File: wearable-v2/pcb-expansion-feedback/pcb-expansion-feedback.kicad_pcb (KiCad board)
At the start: 2 copper layers, 35.1 x 19 mm, 30 parts, among them J16 EA_WF030-39S, J17 JST_AUDIO_OUT, J18 DEBUG_HERALD, J19 FTDI_HERALD, J9 HERALD_V2_CONN_PLUG, U10 ATmega328PB-M, U13 TPA6139A2RGTR, U16 DRV2605LDGSR, U5 MX25R6435FZNIL0, Y2 8Mhz

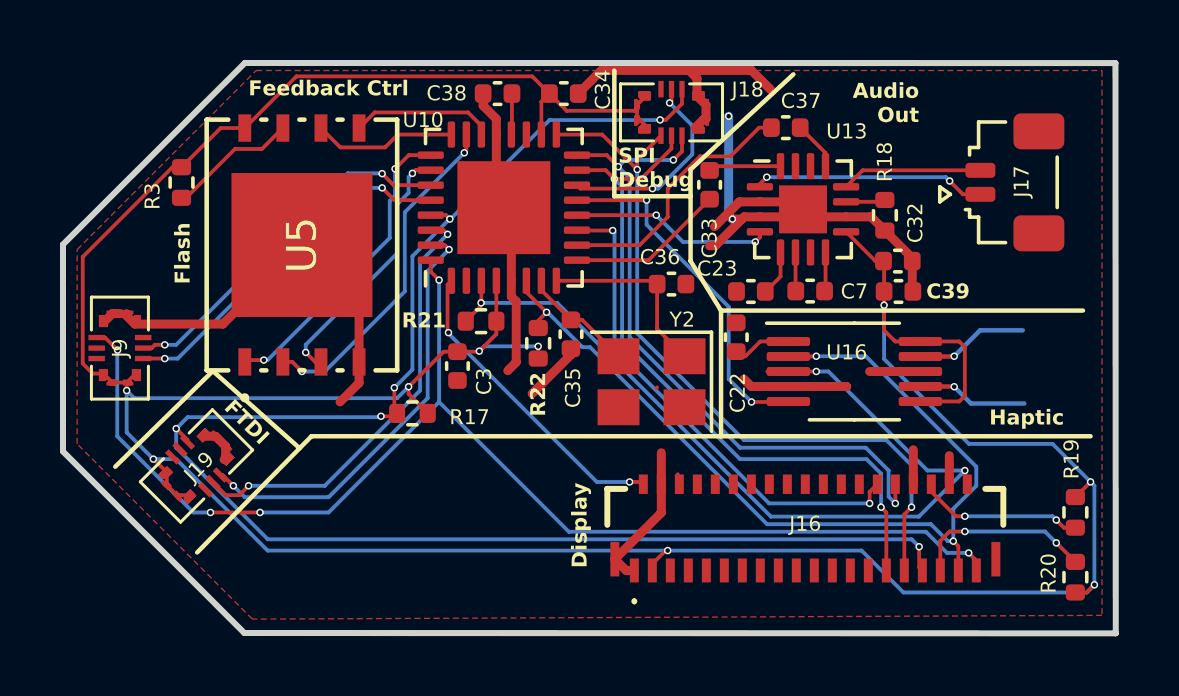
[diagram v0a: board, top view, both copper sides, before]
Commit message: Refactoring PCB files
Moved major boards into their own files.
Corrected design elements for PCBWay manufacture.
Signed-off-by: Adam Fowler <adam@adamfowler.org>
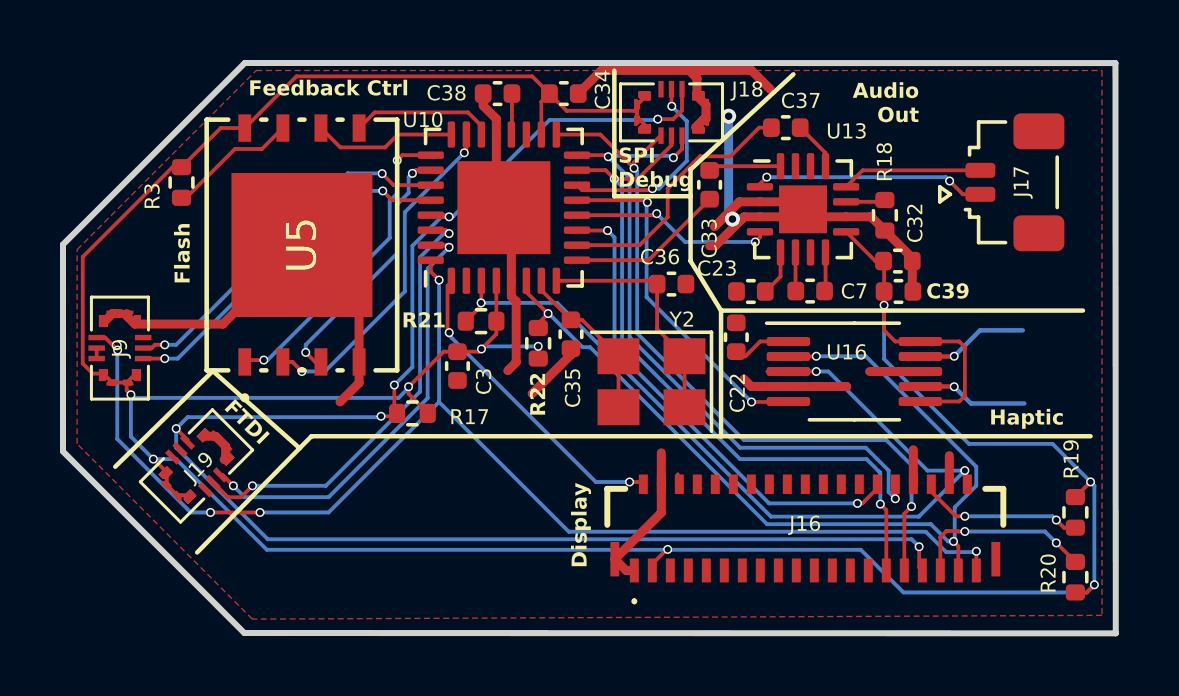
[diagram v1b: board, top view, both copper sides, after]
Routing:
- net Net-(U10-XTAL1/PB6): track 3.80 -> 5.50 mm
- net Net-(U10-XTAL2/PB7): track 6.23 -> 7.89 mm

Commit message: Reworked boards for JLCPCB manufacture
Slightly larger Vias.
Added debug pin holes for Beta testing.
Signed-off-by: Adam Fowler <adam@adamfowler.org>
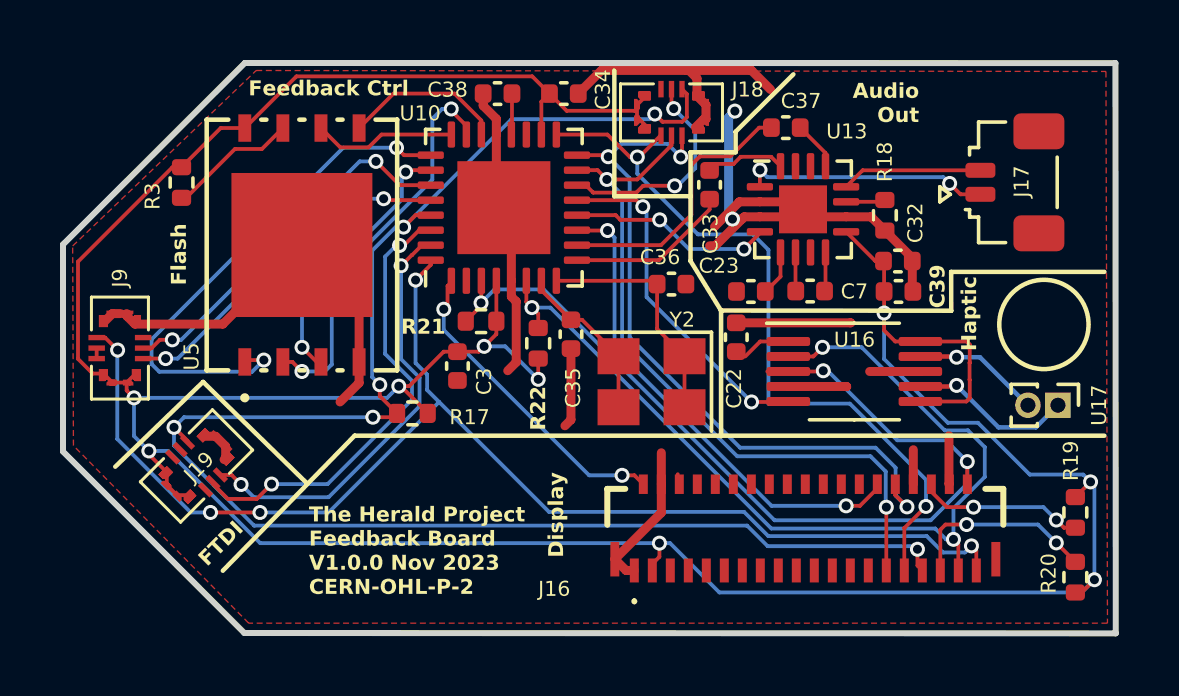
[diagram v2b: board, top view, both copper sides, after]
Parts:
- added U17: VG0832013D, Connector_PinHeader_1.00mm:PinHeader_1x02_P1.00mm_Vertical, F.Cu at (146.9, 90.8)
- J18: value DEBUG_HERALD -> HERALD_V2_CONN_PLUG_ARMSWD
- J19: value FTDI_HERALD -> HERALD_V2_CONN_PLUG
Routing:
- net / Display Board V1/FB_FLASH_SEL: track 10.4 -> 17.5 mm
- net GND: track 68.2 -> 72.0 mm
- net / Display Board V1/FB_AVR_RESET: track 53.8 -> 56.3 mm
- net / Display Board V1/FB_MISO1: track 11.7 -> 13.6 mm
- net / Display Board V1/FB_LRA+: track 3.70 -> 5.48 mm
- net / Display Board V1/DISP_SDO: track 22.4 -> 23.9 mm
- net / Display Board V1/FB_SDA: track 30.0 -> 31.3 mm
- net / Display Board V1/FB_SCL: track 30.9 -> 32.2 mm
- net VDD: track 113.0 -> 114.2 mm
- net / Display Board V1/FB_MOSI1: track 4.77 -> 5.39 mm
- net / Display Board V1/FB_SS0: track 6.74 -> 7.34 mm
- net / Display Board V1/FB_INT: track 42.6 -> 43.2 mm
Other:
- board text added: "The Herald Project Feedback Board V1.0.0 Nov 2023 CERN-OHL-P-2"
